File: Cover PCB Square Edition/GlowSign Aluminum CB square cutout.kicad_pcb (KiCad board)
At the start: 2 copper layers, 175.4 x 88.4 mm, 13 parts, among them P1 Thermal_Pad, P2 Thermal_Pad, P3 Thermal_Pad, P4 Thermal_Pad, P5 Thermal_Pad, P6 Thermal_Pad, U1 SMTSO3030CTJ, U2 SMTSO3030CTJ, U3 SMTSO3030CTJ, U4 SMTSO3030CTJ

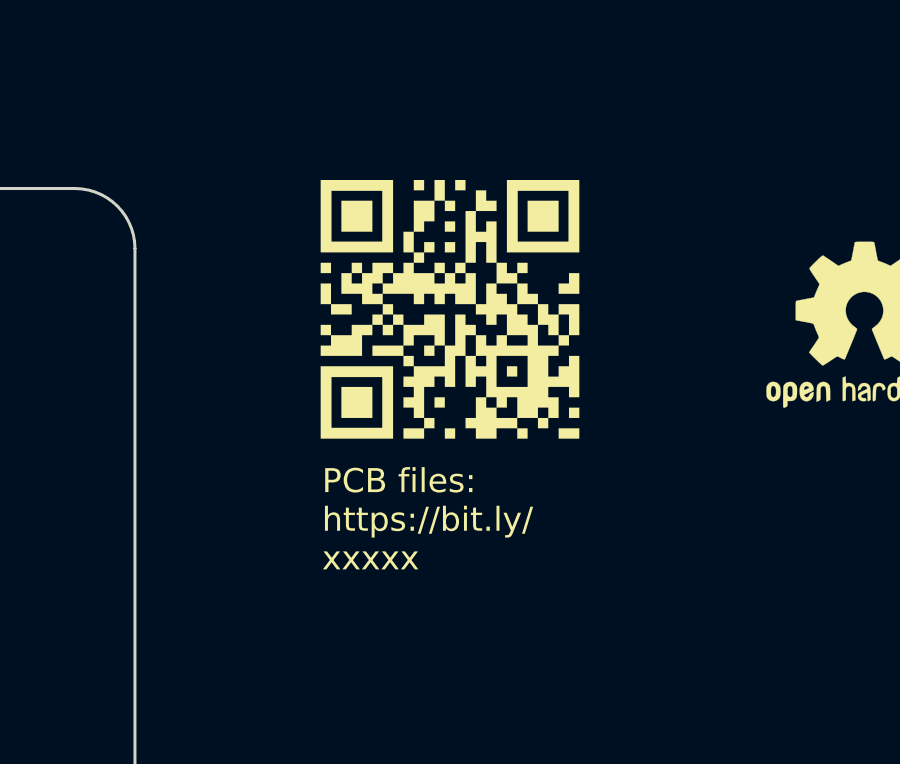
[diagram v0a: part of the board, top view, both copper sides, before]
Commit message: added qr code to cover pcb square
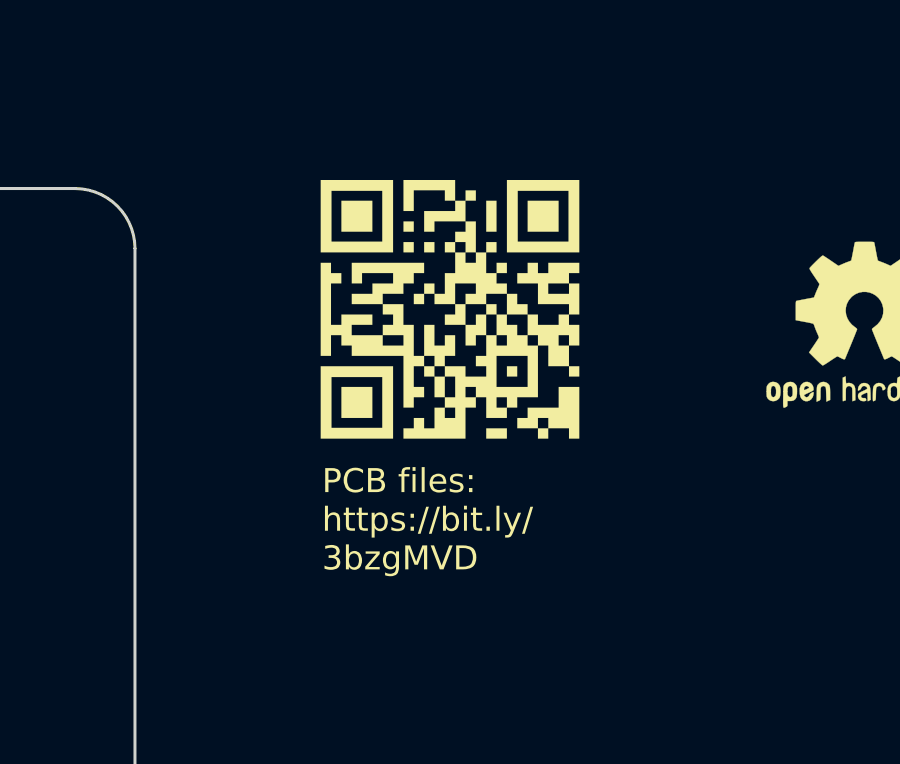
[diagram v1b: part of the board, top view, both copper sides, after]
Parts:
- removed qrcode: LOGO, LOGO
- added G***: LOGO, LOGO, F.Cu at (187.6, 76.1)
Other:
- board text added: "PCB files: https://bit.ly/ 3bzgMVD"
- board text removed: "PCB files: https://bit.ly/ xxxxx"

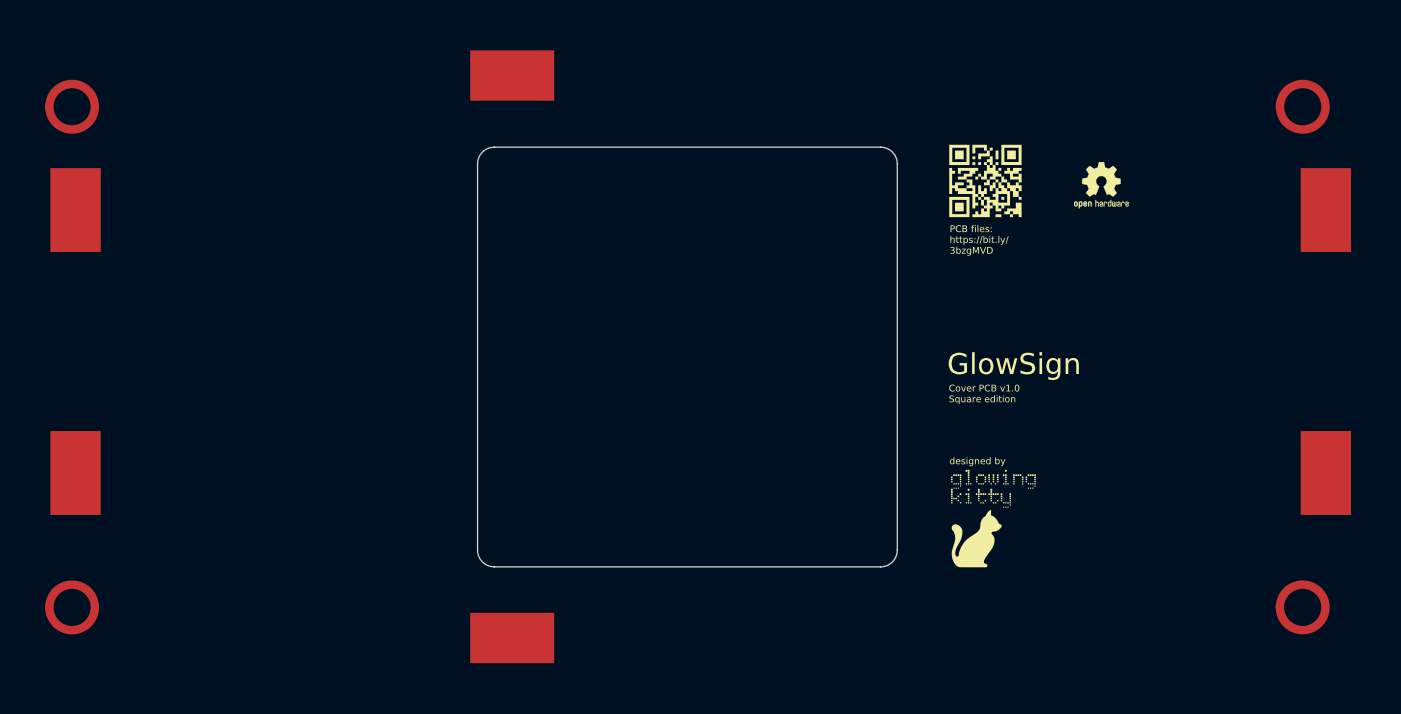
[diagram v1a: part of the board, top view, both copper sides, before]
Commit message: separated battery electronics into separate pcb
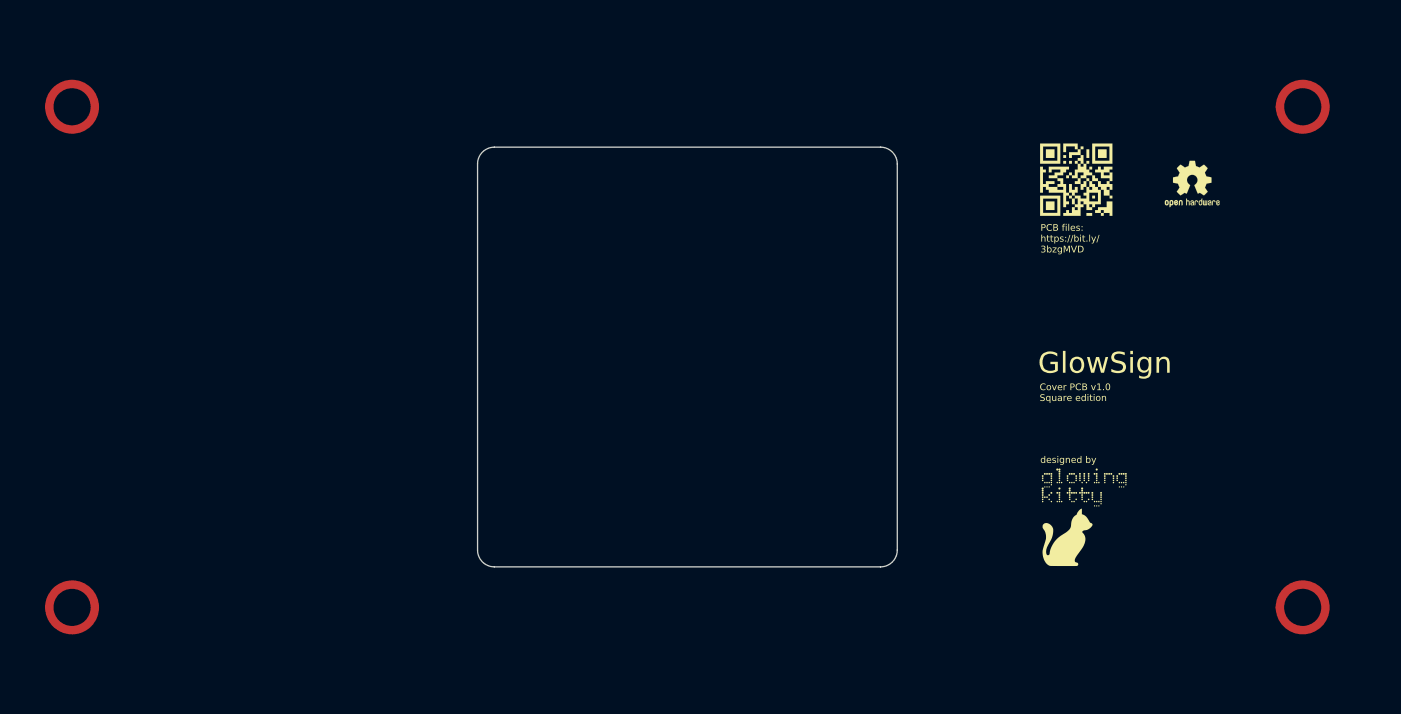
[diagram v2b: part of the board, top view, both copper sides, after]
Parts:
- removed P1, P2, P3, P4, P5, P6: Thermal_Pad, footprint:Thermal pad
- moved G*** 10.8 mm to (198.4, 75.9)
- moved OSHW logo 10.8 mm to (212.2, 76.5)
- moved logo 10.8 mm to (199.2, 115.2)
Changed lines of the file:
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@@
   (net 1 "GND")
   (footprint "LOGO" (layer "F.Cu")
-    (at 188.4172 115.316)
+    (at 199.2376 115.1636)
     (attr board_only exclude_from_pos_files exclude_from_bom)
     (fp_text reference "logo" (at 0 0) (layer "F.SilkS") hide
@@
   )
   (footprint "LOGO" (layer "F.Cu")
-    (at 187.5536 76.0984)
+    (at 198.374 75.946)
     (attr board_only exclude_from_pos_files exclude_from_bom)
     (fp_text reference "G***" (at 0 0) (layer "F.SilkS") hide
@@
       ) (layer "F.SilkS") (width 0) (fill solid))
   )
-  (footprint "footprint:Thermal pad" (layer "F.Cu")
-    (at 132.7162 129.564383 -90)
-    (property "Sheetfile" "GlowSign Aluminum CB square cutout.kicad_sch")
-    (property "Sheetname" "")
-    (property "exclude_from_bom" "")
-    (attr exclude_from_bom)
-    (fp_text reference "P5" (at 0.91 -2.65 -90 unlocked) (layer "F.SilkS") hide
-      (effects (font (size 1 1) (thickness 0.15)))
-    )
-    (fp_text value "Thermal_Pad" (at 0.48 5.74 -90 unlocked) (layer "F.Fab")
-      (effects (font (size 1 1) (thickness 0.15)))
-    )
-    (fp_text user "${REFERENCE}" (at 0.48 7.24 -90 unlocked) (layer "F.Fab")
-      (effects (font (size 1 1) (thickness 0.15)))
-    )
-    (pad "1" smd rect (at 0.9819 1.5354 270) (size 6 10) (layers "F.Cu" "F.Mask")
-      (net 1 "GND") (pintype "bidirectional"))
-  )
-  (footprint "footprint:Thermal pad" (layer "F.Cu")
-    (at 78.1812 78.0288)
-    (property "Sheetfile" "GlowSign Aluminum CB square cutout.kicad_sch")
-    (property "Sheetname" "")
-    (property "exclude_from_bom" "")
-    (attr exclude_from_bom)
-    (fp_text reference "P2" (at 0.91 -2.65 unlocked) (layer "F.SilkS") hide
-      (effects (font (size 1 1) (thickness 0.15)))
-    )
-    (fp_text value "Thermal_Pad" (at 0.48 5.74 unlocked) (layer "F.Fab")
-      (effects (font (size 1 1) (thickness 0.15)))
-    )
-    (fp_text user "${REFERENCE}" (at 0.48 7.24 unlocked) (layer "F.Fab")
-      (effects (font (size 1 1) (thickness 0.15)))
-    )
-    (pad "1" smd rect (at 0.9819 1.5354) (size 6 10) (layers "F.Cu" "F.Mask")
-      (net 1 "GND") (pintype "bidirectional"))
-  )
-  (footprint "footprint:Thermal pad" (layer "F.Cu")
-    (at 129.6454 64.522983 90)
-    (property "Sheetfile" "GlowSign Aluminum CB square cutout.kicad_sch")
-    (property "Sheetname" "")
-    (property "exclude_from_bom" "")
-    (attr exclude_from_bom)
-    (fp_text reference "P3" (at 0.91 -2.65 90 unlocked) (layer "F.SilkS") hide
-      (effects (font (size 1 1) (thickness 0.15)))
-    )
-    (fp_text value "Thermal_Pad" (at 0.48 5.74 90 unlocked) (layer "F.Fab")
-      (effects (font (size 1 1) (thickness 0.15)))
-    )
-    (fp_text user "${REFERENCE}" (at 0.48 7.24 90 unlocked) (layer "F.Fab")
-      (effects (font (size 1 1) (thickness 0.15)))
-    )
-    (pad "1" smd rect (at 0.9819 1.5354 90) (size 6 10) (layers "F.Cu" "F.Mask")
-      (net 1 "GND") (pintype "bidirectional"))
-  )
-  (footprint "footprint:Thermal pad" (layer "F.Cu")
-    (at 227.1253 109.351283)
-    (property "Sheetfile" "GlowSign Aluminum CB square cutout.kicad_sch")
-    (property "Sheetname" "")
-    (property "exclude_from_bom" "")
-    (attr exclude_from_bom)
-    (fp_text reference "P4" (at 0.91 -2.65 unlocked) (layer "F.SilkS") hide
-      (effects (font (size 1 1) (thickness 0.15)))
-    )
-    (fp_text value "Thermal_Pad" (at 0.48 5.74 unlocked) (layer "F.Fab")
-      (effects (font (size 1 1) (thickness 0.15)))
-    )
-    (fp_text user "${REFERENCE}" (at 0.48 7.24 unlocked) (layer "F.Fab")
-      (effects (font (size 1 1) (thickness 0.15)))
-    )
-    (pad "1" smd rect (at 0.9819 1.5354) (size 6 10) (layers "F.Cu" "F.Mask")
-      (net 1 "GND") (pintype "bidirectional"))
-  )
-  (footprint "footprint:Thermal pad" (layer "F.Cu")
-    (at 227.1268 78.0288)
-    (property "Sheetfile" "GlowSign Aluminum CB square cutout.kicad_sch")
-    (property "Sheetname" "")
-    (property "exclude_from_bom" "")
-    (attr exclude_from_bom)
-    (fp_text reference "P6" (at 0.91 -2.65 unlocked) (layer "F.SilkS") hide
-      (effects (font (size 1 1) (thickness 0.15)))
-    )
-    (fp_text value "Thermal_Pad" (at 0.48 5.74 unlocked) (layer "F.Fab")
-      (effects (font (size 1 1) (thickness 0.15)))
-    )
-    (fp_text user "${REFERENCE}" (at 0.48 7.24 unlocked) (layer "F.Fab")
-      (effects (font (size 1 1) (thickness 0.15)))
-    )
-    (pad "1" smd rect (at 0.9819 1.5354) (size 6 10) (layers "F.Cu" "F.Mask")
-      (net 1 "GND") (pintype "bidirectional"))
-  )
   (footprint "footprint:SMTSO3030CTJ No hole" (layer "F.Cu")
     (at 225.3488 67.2592)
@@
   )
   (footprint "Symbol:OSHW-Logo2_7.3x6mm_SilkScreen" (layer "F.Cu")
-    (at 201.3712 76.6064)
+    (at 212.1916 76.454)
     (descr "Open Source Hardware Symbol")
     (tags "Logo Symbol OSHW")
@@
       ) (layer "F.SilkS") (width 0.01) (fill solid))
   )
-  (footprint "footprint:Thermal pad" (layer "F.Cu")
-    (at 78.1797 109.351283)
-    (property "Sheetfile" "GlowSign Aluminum CB square cutout.kicad_sch")
-    (property "Sheetname" "")
-    (property "exclude_from_bom" "")
-    (attr exclude_from_bom)
-    (fp_text reference "P1" (at 0.91 -2.65 unlocked) (layer "F.SilkS") hide
-      (effects (font (size 1 1) (thickness 0.15)))
-    )
-    (fp_text value "Thermal_Pad" (at 0.48 5.74 unlocked) (layer "F.Fab")
-      (effects (font (size 1 1) (thickness 0.15)))
-    )
-    (fp_text user "${REFERENCE}" (at 0.48 7.24 unlocked) (layer "F.Fab")
-      (effects (font (size 1 1) (thickness 0.15)))
-    )
-    (pad "1" smd rect (at 0.9819 1.5354) (size 6 10) (layers "F.Cu" "F.Mask")
-      (net 1 "GND") (pintype "bidirectional"))
-  )
   (footprint "footprint:SMTSO3030CTJ No hole" (layer "F.Cu")
     (at 78.74 67.2592)
@@
   (gr_line (start 239.752648 57.071848) (end 239.752648 137.071848) (layer "User.1") (width 0.1))
   (gr_circle (center 78.752648 126.871848) (end 82.252648 126.871848) (layer "User.1") (width 0.1) (fill none))
-  (gr_text "PCB files:\nhttps://bit.ly/\n3bzgMVD" (at 183.2864 83.1088) (layer "F.SilkS")
+  (gr_text "PCB files:\nhttps://bit.ly/\n3bzgMVD" (at 194.1068 82.9564) (layer "F.SilkS")
     (effects (font (size 0.8 0.8) (thickness 0.15)) (justify left))
   )
-  (gr_text "Cover PCB v1.0\nSquare edition" (at 183.1848 101.4476) (layer "F.SilkS")
+  (gr_text "Cover PCB v1.0\nSquare edition" (at 194.0052 101.2952) (layer "F.SilkS")
     (effects (font (size 0.8 0.8) (thickness 0.15)) (justify left))
   )
-  (gr_text "designed by" (at 183.261 109.474) (layer "F.SilkS")
+  (gr_text "designed by" (at 194.0814 109.3216) (layer "F.SilkS")
     (effects (font (size 0.8 0.8) (thickness 0.15)) (justify left))
   )
-  (gr_text "GlowSign" (at 182.9816 97.9424) (layer "F.SilkS")
+  (gr_text "GlowSign" (at 193.802 97.79) (layer "F.SilkS")
     (effects (font (size 2.5 2.5) (thickness 0.4)) (justify left))
   )
